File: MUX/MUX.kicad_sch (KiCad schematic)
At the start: 134 parts, among them P1 Conn_02x36_Top_Bottom, P2 DB9_Male, P3 DB9_Male, P4 DB9_Male, P5 DB9_Male

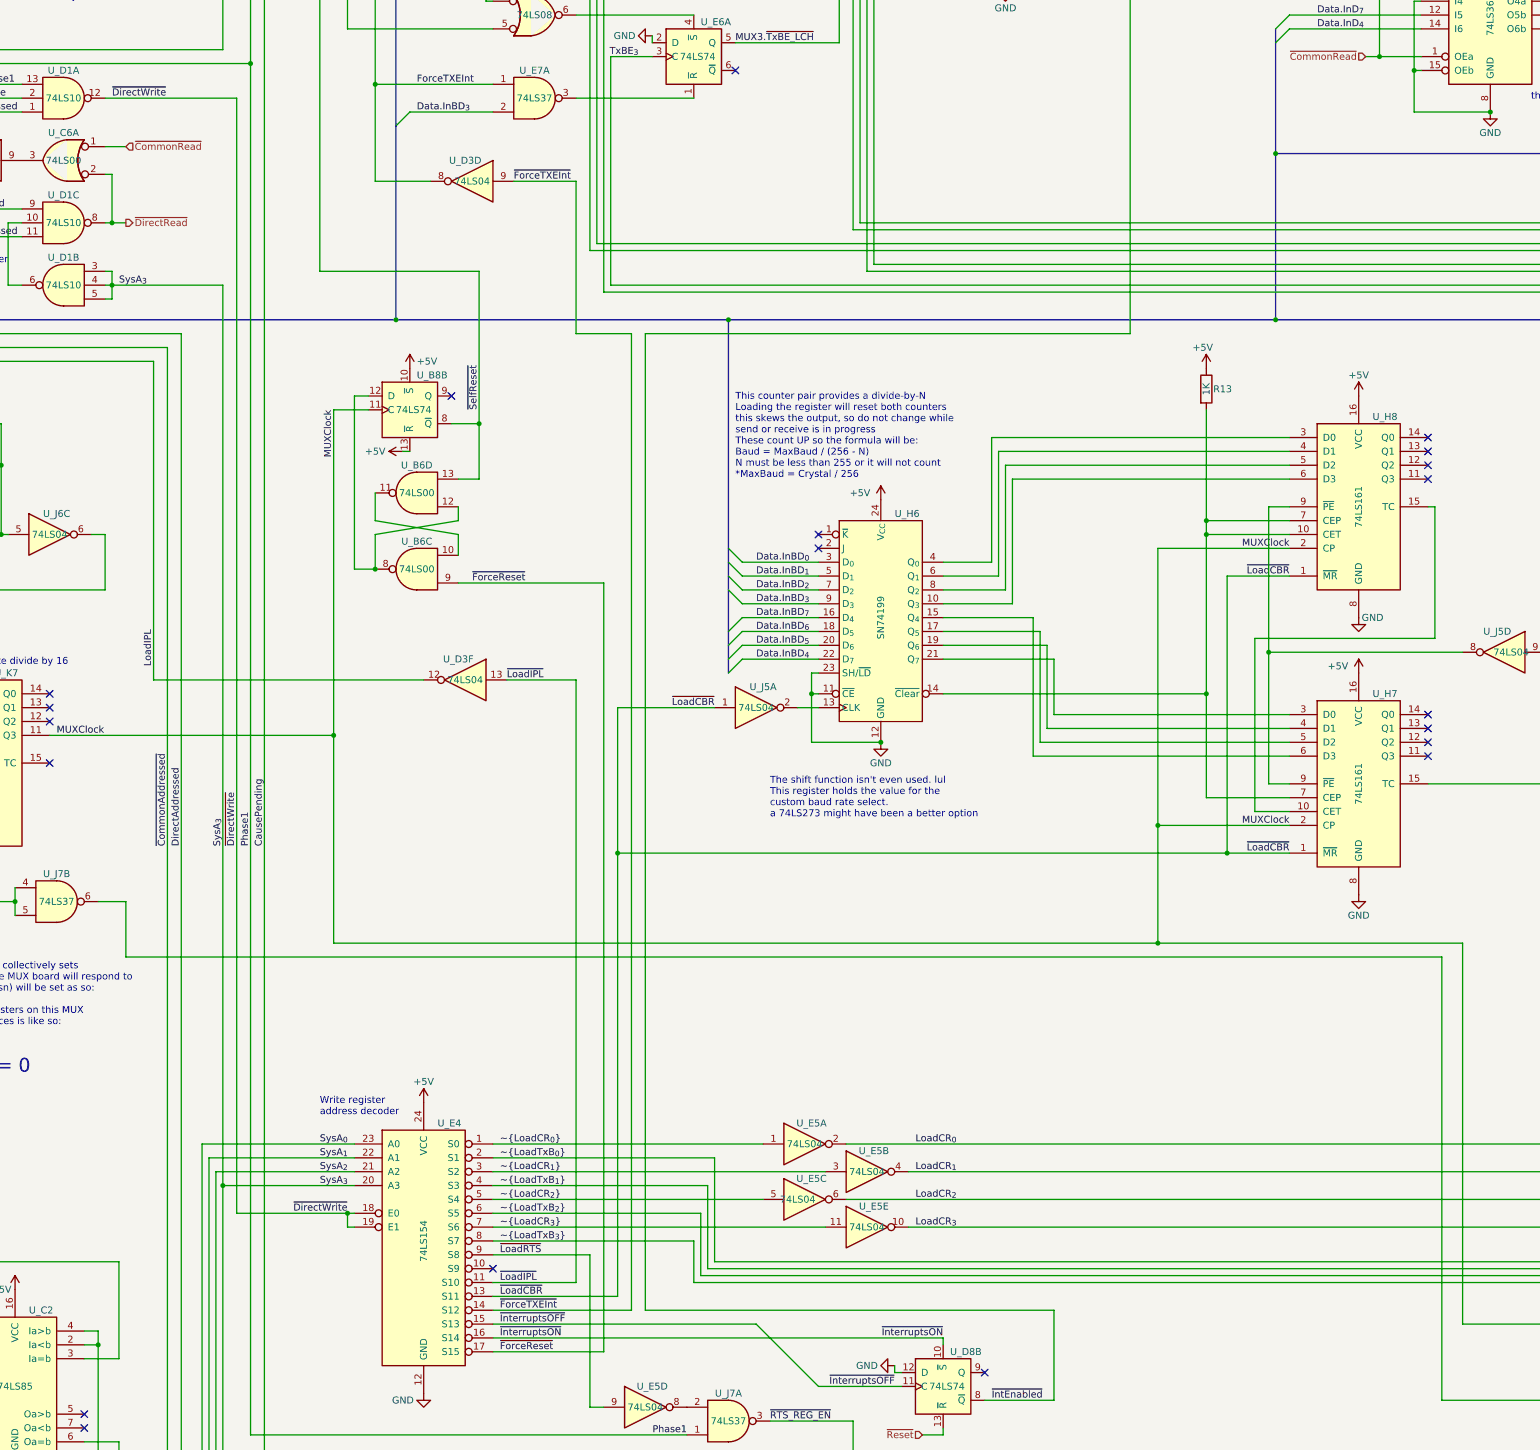
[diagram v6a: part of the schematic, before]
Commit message: MUX: Avoid more unobtanium chips
- Replaced U_H6 with LS273
- Allow using russian К1533ИД3 as U_E4; it has narrow DIP package
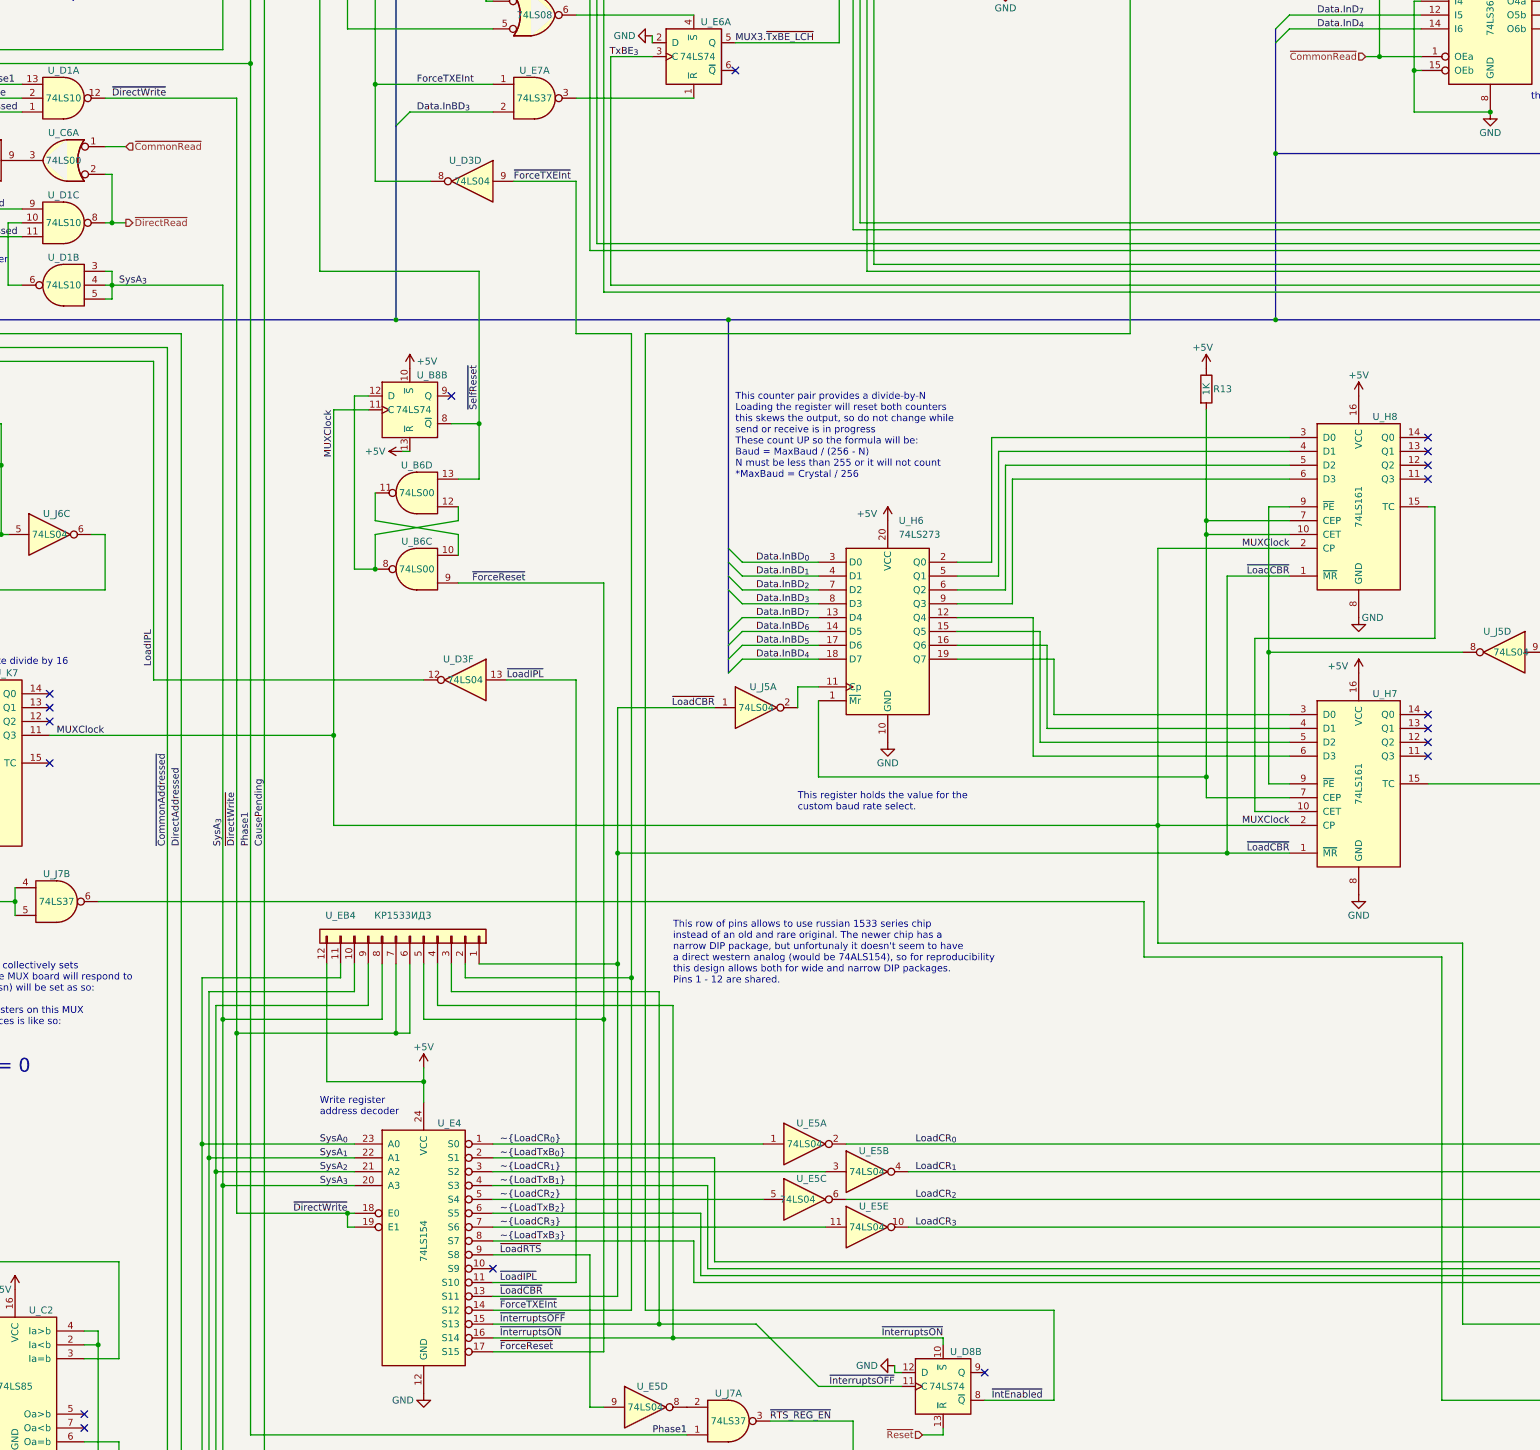
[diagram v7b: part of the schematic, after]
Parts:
- removed U_H6: SN74199, Package_DIP:DIP-24_W15.24mm, symbol 74xx:SN74199
- added U_EB4: КР1533ИД3, Connector_PinHeader_2.54mm:PinHeader_1x12_P2.54mm_Vertical, symbol Connector_Generic:Conn_01x12
- added U_H6: 74LS273, Package_DIP:DIP-20_W7.62mm, symbol 74xx:74LS273
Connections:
- net +5V: now also U_EB4.12 (Pin_12), U_H6.20 (VCC)
- net Data.InBD_{0}: now also U_H6.3 (D0)
- net Data.InBD_{1}: now also U_H6.4 (D1)
- net Data.InBD_{2}: now also U_H6.7 (D2)
- net Data.InBD_{3}: now also U_H6.8 (D3)
- net Data.InBD_{4}: now also U_H6.18 (D7)
- net Data.InBD_{5}: now also U_H6.17 (D6)
- net Data.InBD_{6}: now also U_H6.14 (D5)
- net Data.InBD_{7}: now also U_H6.13 (D4)
- net GND: now also U_H6.10 (GND)
- net SysA_{0}: now also U_EB4.11 (Pin_11)
- net SysA_{1}: now also U_EB4.10 (Pin_10)
- net SysA_{2}: now also U_EB4.9 (Pin_9)
- net SysA_{3}: now also U_EB4.8 (Pin_8)
- net ~{DirectWrite}: now also U_EB4.6 (Pin_6), U_EB4.7 (Pin_7)
- net ~{ForceReset}: now also U_EB4.5 (Pin_5)
- net ~{ForceTXEInt}: now also U_EB4.2 (Pin_2)
- net ~{InterruptsOFF}: now also U_EB4.3 (Pin_3)
- net ~{InterruptsON}: now also U_EB4.4 (Pin_4)
- net ~{LoadCBR}: now also U_EB4.1 (Pin_1)
- net at R13.2, U_H7.7 (CEP), U_H8.10 (CET)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: now also U_H6.1 (~{Mr})
- net at U_H8.3 (D0): now also U_H6.2 (Q0)
- net at U_H8.4 (D1): now also U_H6.5 (Q1)
- net at U_H8.5 (D2): now also U_H6.6 (Q2)
- net at U_H8.6 (D3): now also U_H6.9 (Q3)
- net at U_J5.2: now also U_H6.11 (Cp)
- net at U_H7.6 (D3): now also U_H6.12 (Q4)
- net at U_H7.5 (D2): now also U_H6.15 (Q5)
- net at U_H7.4 (D1): now also U_H6.16 (Q6)
- net at U_H7.3 (D0): now also U_H6.19 (Q7)
- no-connect marks 136 -> 134
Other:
- note added: "This register holds the value for the custom baud rate select."
- note added: "This row of pins allows to use russian 1533 series chip instead of an old and rare original. The newer chip has a narrow DIP package, but unfortunaly it doesn't seem to have a direct western analog (would be 74ALS154), so for reproducibility this design allows both for wide and narrow DIP packages. Pins 1 - 12 are shared."
- note removed: "The shift function isn't even used. lul This register holds the value for the custom baud rate select. a 74LS273 might have been a better option"

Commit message: MUX: Add connector pinout switch jumpers
Provide jumper blocks to easily confiure MUX outputs as either Centuriobn native
or standard RS232 pinout. Provides for ease of use of USB adapters,
off-the-shelf cables, etc.
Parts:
- added JP1, JP2, JP3, JP4: Jumper_3x9_Bridged12, Connector_PinHeader_2.54mm:PinHeader_3x09_P2.54mm_Vertical, symbol Jumper:Jumper_3_Bridged12
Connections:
- net -12V: now also JP1.14 (C5), JP2.14 (C5), JP3.14 (C5), JP4.14 (C5); no longer P2.3, P3.3, P4.3, P5.3
- net GND: now also JP1.26 (C9), JP2.26 (C9), JP3.26 (C9), JP4.26 (C9); no longer P2.1, P3.1, P4.1, P5.1
- net ~{CTS_{0}}: now also JP1.20 (C7); no longer P2.2
- net ~{CTS_{1}}: now also JP2.20 (C7); no longer P3.2
- net ~{CTS_{2}}: now also JP3.20 (C7); no longer P4.2
- net ~{CTS_{3}}: now also JP4.20 (C7); no longer P5.2
- net ~{RTS_{0}}: now also JP1.8 (C3); no longer P2.4
- net ~{RTS_{1}}: now also JP2.8 (C3); no longer P3.4
- net ~{RTS_{2}}: now also JP3.8 (C3); no longer P4.4
- net ~{RTS_{3}}: now also JP4.8 (C3); no longer P5.4
- net ~{RX_{0}}: now also JP1.11 (C4); no longer P2.8
- net ~{RX_{1}}: now also JP2.11 (C4); no longer P3.8
- net ~{RX_{2}}: now also JP3.11 (C4); no longer P4.8
- net ~{RX_{3}}: now also JP4.11 (C4); no longer P5.8
- net ~{TX_{0}_EIA}: now also JP1.17 (C6); no longer P2.7
- net ~{TX_{0}}: now also JP1.23 (C8); no longer P2.6
- net ~{TX_{1}_EIA}: now also JP2.17 (C6); no longer P3.7
- net ~{TX_{1}}: now also JP2.23 (C8); no longer P3.6
- net ~{TX_{2}_EIA}: now also JP3.17 (C6); no longer P4.7
- net ~{TX_{2}}: now also JP3.23 (C8); no longer P4.6
- net ~{TX_{3}_EIA}: now also P5.2, JP4.12 (B4), JP4.17 (C6), JP4.19 (A7); no longer P5.7
- net ~{TX_{3}}: now also JP4.23 (C8); no longer P5.6
- net at R4.2: now also JP2.5 (C2); no longer P3.9
- net at R8.2: now also JP3.5 (C2); no longer P4.9
- net at P3.5: now also JP2.1 (A1), JP2.27 (B9); no longer R3.2
- net at R5.2: now also JP3.2 (C1); no longer P4.5
- net at P5.5: now also JP4.1 (A1), JP4.27 (B9); no longer R10.2
- net at P5.9: now also JP4.4 (A2); no longer R7.2
- net at P2.5: now also JP1.1 (A1), JP1.27 (B9); no longer R1.2
- net at P2.9: now also JP1.4 (A2); no longer R2.2
- new net: JP2.10 (A4), JP2.21 (B7), P3.8
- new net: JP2.12 (B4), JP2.19 (A7), P3.2
- new net: JP2.13 (A5), JP2.24 (B8), P3.3
- new net: JP2.16 (A6), JP2.9 (B3), P3.7
- new net: JP2.2 (C1), R3.2
- new net: JP2.22 (A8), P3.6
- new net: JP2.25 (A9), P3.1
- new net: JP2.4 (A2), P3.9
- new net: JP2.7 (A3), P3.4
- new net: JP4.25 (A9), P5.1
- new net: JP4.13 (A5), JP4.24 (B8), P5.3
- new net: JP4.7 (A3), P5.4
- new net: JP4.22 (A8), P5.6
- new net: JP4.16 (A6), JP4.9 (B3), P5.7
- new net: JP4.10 (A4), JP4.21 (B7), P5.8
- new net: JP1.10 (A4), JP1.21 (B7), P2.8
- new net: JP1.12 (B4), JP1.19 (A7), P2.2
- new net: JP1.13 (A5), JP1.24 (B8), P2.3
- new net: JP1.16 (A6), JP1.9 (B3), P2.7
- new net: JP1.2 (C1), R1.2
- new net: JP1.22 (A8), P2.6
- new net: JP1.25 (A9), P2.1
- new net: JP1.5 (C2), R2.2
- new net: JP1.7 (A3), P2.4
- new net: JP3.25 (A9), P4.1
- new net: JP3.12 (B4), JP3.19 (A7), P4.2
- new net: JP3.13 (A5), JP3.24 (B8), P4.3
- new net: JP3.7 (A3), P4.4
- new net: JP3.1 (A1), JP3.27 (B9), P4.5
- new net: JP3.22 (A8), P4.6
- new net: JP3.16 (A6), JP3.9 (B3), P4.7
- new net: JP3.10 (A4), JP3.21 (B7), P4.8
- new net: JP3.4 (A2), P4.9
- new net: JP4.2 (C1), R10.2
- new net: JP4.5 (C2), R7.2
- no-connect marks 134 -> 150
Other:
- note added: "These jumper blocks provides easy switch between original Centurion and standard RS-232 pinouts. Shown in "Centurion" position."
- moved on the sheet: P2, P3, P4, P5, R1, R10, R2, R3, R4, R5, R7, R8
